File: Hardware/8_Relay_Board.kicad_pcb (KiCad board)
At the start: 4 copper layers, 74.9 x 81.3 mm, 73 parts, among them J1 Conn_01x09, J10 Screw_Terminal_3.5mm_2, J2 Conn_01x09, J3 Screw_Terminal_3.5mm_4, J4 Screw_Terminal_3.5mm_4, J5 Screw_Terminal_3.5mm_4, J6 Screw_Terminal_3.5mm_4, J7 Screw_Terminal_3.5mm_4, J8 Screw_Terminal_3.5mm_4, J9 Barrel_Jack, U1 TLP627-4, U2 TLP627-4

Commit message: Close to finishing layout
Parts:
- removed J9: Barrel_Jack, SparkFun-Connector:POWER_JACK_PTH
- added J11: USB_C_Receptacle, SparkFun-Connector:USB-C-16P, F.Cu at (168.9, 144.8)
- added R18: 5.1k, SparkFun-Resistor:R_0603_1608Metric, F.Cu at (170.2, 141.0)
- added R19: 5.1k, SparkFun-Resistor:R_0603_1608Metric, F.Cu at (167.6, 141.0)
- added U3: TLP627, SparkFun-Semiconductor-Standard:DIP4, F.Cu at (110.5, 137.2)
- added U4: TLP627, SparkFun-Semiconductor-Standard:DIP4, F.Cu at (129.5, 137.2)
- added U5: TLP627, SparkFun-Semiconductor-Standard:DIP4, F.Cu at (135.9, 137.2)
- added U6: TLP627, SparkFun-Semiconductor-Standard:DIP4, F.Cu at (142.2, 137.2)
- added U8: TLP627, SparkFun-Semiconductor-Standard:DIP4, F.Cu at (148.6, 137.2)
- added U9: TLP627, SparkFun-Semiconductor-Standard:DIP4, F.Cu at (154.9, 137.2)
- added kibuzzard-6524CD2A: G***, kibuzzard-6524CD2A, F.Cu at (101.5, 91.2)
- added kibuzzard-6524CD2A: G***, kibuzzard-6524CD2A, F.Cu at (101.5, 80.6)
- added kibuzzard-6524CD2A: G***, kibuzzard-6524CD2A, F.Cu at (183.0, 98.2)
- added kibuzzard-6524CD2A: G***, kibuzzard-6524CD2A, F.Cu at (183.0, 119.1)
- added kibuzzard-6524CD2A: G***, kibuzzard-6524CD2A, F.Cu at (183.0, 87.6)
- added kibuzzard-6524CD2A: G***, kibuzzard-6524CD2A, F.Cu at (101.5, 101.7)
- added kibuzzard-6524CD2A: G***, kibuzzard-6524CD2A, F.Cu at (183.0, 108.6)
- added kibuzzard-6524CD2A: G***, kibuzzard-6524CD2A, F.Cu at (101.5, 112.1)
- added kibuzzard-6524CD3E: G***, kibuzzard-6524CD3E, F.Cu at (101.5, 84.1)
- added kibuzzard-6524CD3E: G***, kibuzzard-6524CD3E, F.Cu at (101.5, 115.6)
- added kibuzzard-6524CD3E: G***, kibuzzard-6524CD3E, F.Cu at (101.5, 94.6)
- added kibuzzard-6524CD3E: G***, kibuzzard-6524CD3E, F.Cu at (183.0, 105.0)
- added kibuzzard-6524CD3E: G***, kibuzzard-6524CD3E, F.Cu at (101.5, 105.2)
- added kibuzzard-6524CD3E: G***, kibuzzard-6524CD3E, F.Cu at (183.0, 94.6)
- added kibuzzard-6524CD3E: G***, kibuzzard-6524CD3E, F.Cu at (183.0, 115.6)
- added kibuzzard-6524CD3E: G***, kibuzzard-6524CD3E, F.Cu at (183.0, 84.1)
- added kibuzzard-6524CD4E: G***, kibuzzard-6524CD4E, F.Cu at (183.0, 91.2)
- added kibuzzard-6524CD4E: G***, kibuzzard-6524CD4E, F.Cu at (183.0, 112.1)
- added kibuzzard-6524CD4E: G***, kibuzzard-6524CD4E, F.Cu at (101.5, 119.1)
- added kibuzzard-6524CD4E: G***, kibuzzard-6524CD4E, F.Cu at (101.5, 87.6)
- added kibuzzard-6524CD4E: G***, kibuzzard-6524CD4E, F.Cu at (101.5, 98.2)
- added kibuzzard-6524CD4E: G***, kibuzzard-6524CD4E, F.Cu at (183.0, 101.6)
- added kibuzzard-6524CD4E: G***, kibuzzard-6524CD4E, F.Cu at (101.5, 108.7)
- added kibuzzard-6524CD4E: G***, kibuzzard-6524CD4E, F.Cu at (183.0, 80.6)
- JP9: moved to B.Cu
- U1, U2: value TLP627-4 -> TLP627; footprint SparkFun-Semiconductor-Standard:PDIP16 -> SparkFun-Semiconductor-Standard:DIP4
- U7: footprint SparkFun-Aesthetic:Ordering_Instructions -> SparkFun-Aesthetic:ORDERING_INSTRUCTIONS
- moved U1 29.6 mm to (116.8, 137.2), turned to 90 degrees
- moved ST1 9.52 mm to (183.5, 73.7)
- moved ST2 9.52 mm to (183.5, 149.9)
- moved FID1 8.89 mm to (179.1, 151.1)
- moved FID4 8.89 mm to (179.1, 151.1)
- moved U2 8.13 mm to (123.2, 137.2), turned to 90 degrees
- moved R12 6.48 mm to (132.1, 141.0)
- moved J1 6.35 mm to (138.4, 151.1)
- moved J2 6.35 mm to (138.4, 148.6)
- moved JP5 5.39 mm to (148.6, 116.8)
- moved JP6 5.39 mm to (148.6, 104.1)
- moved JP7 5.39 mm to (148.6, 91.4)
- moved JP8 5.39 mm to (148.6, 78.7)
- moved R11 5.24 mm to (125.7, 141.0)
- moved J10 5.08 mm to (152.7, 148.6)
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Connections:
- J3 pad 1: NO1 -> COM1
- J3 pad 2: COM1 -> NC1
- J3 pad 3: NC1 -> NO1
- J3 pad 4: NO2 -> COM2
- J4 pad 1: COM2 -> NC2
- J4 pad 2: NC2 -> NO2
- J4 pad 3: NO3 -> COM3
- J4 pad 4: COM3 -> NC3
- J5 pad 1: NC3 -> NO3
- J5 pad 2: NO4 -> COM4
- J5 pad 3: COM4 -> NC4
- J5 pad 4: NC4 -> NO4
- J6 pad 1: NO5 -> COM5
- J6 pad 2: COM5 -> NC5
- J6 pad 3: NC5 -> NO5
- J6 pad 4: NO6 -> COM6
- J7 pad 1: COM6 -> NC6
- J7 pad 2: NC6 -> NO6
- J7 pad 3: NO7 -> COM7
- J7 pad 4: COM7 -> NC7
- J8 pad 1: NC7 -> NO7
- J8 pad 2: NO8 -> COM8
- J8 pad 3: COM8 -> NC8
- J8 pad 4: NC8 -> NO8
- U1 pad 1: IN5 -> IN2
- U1 pad 2: Net-(R13-Pad2) -> Net-(R10-Pad2)
- U1 pad 3: IN6 -> GND
- U1 pad 4: Net-(R14-Pad2) -> RELAY3
- U2 pad 1: IN1 -> IN3
- U2 pad 2: Net-(R9-Pad2) -> Net-(R11-Pad2)
- U2 pad 3: IN2 -> GND
- U2 pad 4: Net-(R10-Pad2) -> RELAY2
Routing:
- net +5V: track 20.8 -> 282.8 mm, vias 0 -> 10
- net RELAY1: track 0.00 -> 82.7 mm
- net RELAY2: track 0.00 -> 67.0 mm, vias 0 -> 1
- net RELAY8: track 0.00 -> 65.2 mm
- net RELAY3: track 0.00 -> 58.3 mm, vias 0 -> 1
- net RELAY4: track 0.00 -> 48.8 mm, vias 0 -> 1
- net RELAY7: track 0.00 -> 48.8 mm
- net RELAY6: track 0.00 -> 35.7 mm
- net NC1: track 0.00 -> 17.8 mm
- net NC8: track 0.00 -> 16.8 mm
- net NC2: track 0.00 -> 16.1 mm
- net NC7: track 0.00 -> 15.9 mm
- net RELAY5: track 0.00 -> 15.8 mm
- net NC4: track 0.00 -> 15.3 mm
- net NC3: track 0.00 -> 15.2 mm
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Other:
- board size 74.9 x 81.3 mm -> 87.6 x 81.3 mm
- board text added: "Layers: 2"
- board text removed: "Controlled Impedance: JLC7628"
- board text removed: "Finish: ENIG"
- board text removed: "Layers: 4"
- board text removed: "Material: TG155"
- board text removed: "No Clean Process"

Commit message: Ready for final review
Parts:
- removed kibuzzard-6524CD2A (x8): G***, kibuzzard-6524CD2A
- removed kibuzzard-6524CD3E (x8): G***, kibuzzard-6524CD3E
- removed kibuzzard-6524CD4E (x8): G***, kibuzzard-6524CD4E
- added G***: LOGO, SparkFun-Aesthetic:SparkX_Logo_8mm, F.Cu at (175.3, 134.4)
- added G***: LOGO, SparkFun-Aesthetic:SparkX_Logo_8mm, B.Cu at (142.2, 130.0)
- added kibuzzard-65297156: G***, kibuzzard-65297156, F.Cu at (140.7, 121.9)
- added kibuzzard-65297156: G***, kibuzzard-65297156, B.Cu at (126.2, 116.3)
- added kibuzzard-65297163: G***, kibuzzard-65297163, F.Cu at (140.2, 107.7)
- added kibuzzard-65297163: G***, kibuzzard-65297163, B.Cu at (126.0, 103.9)
- added kibuzzard-6529717D: G***, kibuzzard-6529717D, F.Cu at (140.2, 95.0)
- added kibuzzard-6529717D: G***, kibuzzard-6529717D, B.Cu at (126.0, 91.4)
- added kibuzzard-65297189: G***, kibuzzard-65297189, F.Cu at (140.2, 82.3)
- added kibuzzard-65297189: G***, kibuzzard-65297189, B.Cu at (126.0, 79.0)
- added kibuzzard-65297199: G***, kibuzzard-65297199, F.Cu at (144.8, 74.2)
- added kibuzzard-65297199: G***, kibuzzard-65297199, B.Cu at (158.8, 78.7)
- added kibuzzard-652971A7: G***, kibuzzard-652971A7, F.Cu at (144.3, 87.9)
- added kibuzzard-652971A7: G***, kibuzzard-652971A7, B.Cu at (158.8, 91.4)
- added kibuzzard-652971AD: G***, kibuzzard-652971AD, F.Cu at (144.8, 100.6)
- added kibuzzard-652971AD: G***, kibuzzard-652971AD, B.Cu at (158.8, 104.4)
- added kibuzzard-652971B3: G***, kibuzzard-652971B3, F.Cu at (144.3, 113.3)
- added kibuzzard-652971B3: G***, kibuzzard-652971B3, B.Cu at (158.8, 116.6)
- added kibuzzard-65297316: G***, kibuzzard-65297316, F.Cu at (118.1, 146.1)
- added kibuzzard-65297316: G***, kibuzzard-65297316, B.Cu at (118.1, 146.1)
- added kibuzzard-65297321: G***, kibuzzard-65297321, F.Cu at (120.7, 146.1)
- added kibuzzard-65297321: G***, kibuzzard-65297321, B.Cu at (120.7, 146.1)
- added kibuzzard-65297327: G***, kibuzzard-65297327, F.Cu at (123.2, 146.1)
- added kibuzzard-65297327: G***, kibuzzard-65297327, B.Cu at (123.2, 146.1)
- added kibuzzard-6529732E: G***, kibuzzard-6529732E, F.Cu at (125.7, 146.1)
- added kibuzzard-6529732E: G***, kibuzzard-6529732E, B.Cu at (125.7, 146.1)
- added kibuzzard-65297338: G***, kibuzzard-65297338, F.Cu at (128.3, 146.1)
- added kibuzzard-65297338: G***, kibuzzard-65297338, B.Cu at (128.3, 146.1)
- added kibuzzard-6529733E: G***, kibuzzard-6529733E, F.Cu at (130.8, 146.1)
- added kibuzzard-6529733E: G***, kibuzzard-6529733E, B.Cu at (130.8, 146.1)
- added kibuzzard-65297343: G***, kibuzzard-65297343, F.Cu at (133.3, 146.1)
- added kibuzzard-65297343: G***, kibuzzard-65297343, B.Cu at (133.3, 146.1)
- added kibuzzard-6529734A: G***, kibuzzard-6529734A, F.Cu at (135.9, 146.1)
- added kibuzzard-6529734A: G***, kibuzzard-6529734A, B.Cu at (135.9, 146.1)
- added kibuzzard-65297353: G***, kibuzzard-65297353, F.Cu at (138.4, 146.7)
- added kibuzzard-65297353: G***, kibuzzard-65297353, B.Cu at (138.4, 146.7)
- added kibuzzard-652973B2: G***, kibuzzard-652973B2, F.Cu at (130.2, 151.1)
- added kibuzzard-652973E9: G***, kibuzzard-652973E9, F.Cu at (168.9, 130.2)
- added kibuzzard-65297443: G***, kibuzzard-65297443, F.Cu at (152.7, 143.5)
- added kibuzzard-65297443: G***, kibuzzard-65297443, B.Cu at (152.7, 143.5)
- added kibuzzard-65297450: G***, kibuzzard-65297450, F.Cu at (156.2, 143.5)
- added kibuzzard-65297450: G***, kibuzzard-65297450, B.Cu at (156.2, 143.5)
- added kibuzzard-65298D3A: G***, kibuzzard-65298D3A, F.Cu at (161.3, 148.8)
- added kibuzzard-65298D3A: G***, kibuzzard-65298D3A, B.Cu at (161.0, 148.8)
- added kibuzzard-652991A0: G***, kibuzzard-652991A0, B.Cu at (130.3, 151.1)
- added kibuzzard-652997F8: G***, kibuzzard-652997F8, F.Cu at (179.3, 134.6)
- added kibuzzard-65299803: G***, kibuzzard-65299803, F.Cu at (182.4, 134.6)
- added kibuzzard-6529980A: G***, kibuzzard-6529980A, B.Cu at (142.0, 134.1)
- added kibuzzard-65299816: G***, kibuzzard-65299816, B.Cu at (142.0, 137.2)
- U1, U2, U3, U4, U5, U6, U8, U9: footprint SparkFun-Semiconductor-Standard:DIP4 -> SparkFun-Semiconductor-Standard:SMDIP4
- moved U3 4.02 mm to (111.8, 133.3)
- moved U4 4.02 mm to (130.8, 133.3)
- moved U5 4.02 mm to (137.2, 133.3)
- moved U8 4.02 mm to (149.9, 133.3)
- moved U9 4.02 mm to (156.2, 133.3)
- moved U1 4.02 mm to (118.1, 133.3)
- moved U2 4.02 mm to (124.5, 133.3)
- moved U6 4.02 mm to (143.5, 133.3)
- moved J1 2.54 mm to (138.4, 148.6)
- moved J2 2.54 mm to (138.4, 151.1)
- moved J11 1.21 mm to (168.9, 146.0)
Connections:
- J3 pad 1: COM1 -> NC1
- J3 pad 2: NC1 -> COM1
- J3 pad 4: COM2 -> NC2
- J4 pad 1: NC2 -> COM2
- J4 pad 3: COM3 -> NC3
- J4 pad 4: NC3 -> COM3
- J5 pad 2: COM4 -> NC4
- J5 pad 3: NC4 -> COM4
- J6 pad 1: COM5 -> NC5
- J6 pad 2: NC5 -> COM5
- J6 pad 4: COM6 -> NC6
- J7 pad 1: NC6 -> COM6
- J7 pad 3: COM7 -> NC7
- J7 pad 4: NC7 -> COM7
- J8 pad 2: COM8 -> NC8
- J8 pad 3: NC8 -> COM8
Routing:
- net +5V: track 282.8 -> 287.8 mm
- net COM1: track 12.3 -> 15.9 mm
- net IN3: track 14.9 -> 11.4 mm
- net GND: track 1.85 -> 4.94 mm
- net COM8: track 13.3 -> 10.3 mm
- net IN2: track 15.5 -> 13.0 mm
- net IN7: track 25.5 -> 23.0 mm
- net IN4: track 15.5 -> 13.0 mm
- net NC1: track 17.8 -> 15.9 mm
- net IN6: track 20.9 -> 19.1 mm
- net NC4: track 15.3 -> 16.7 mm
- net NC8: track 16.8 -> 18.2 mm
- net COM3: track 10.4 -> 11.9 mm
- net COM2: track 11.3 -> 12.8 mm
- net COM5: track 10.3 -> 11.7 mm
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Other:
- board text added: "x01"

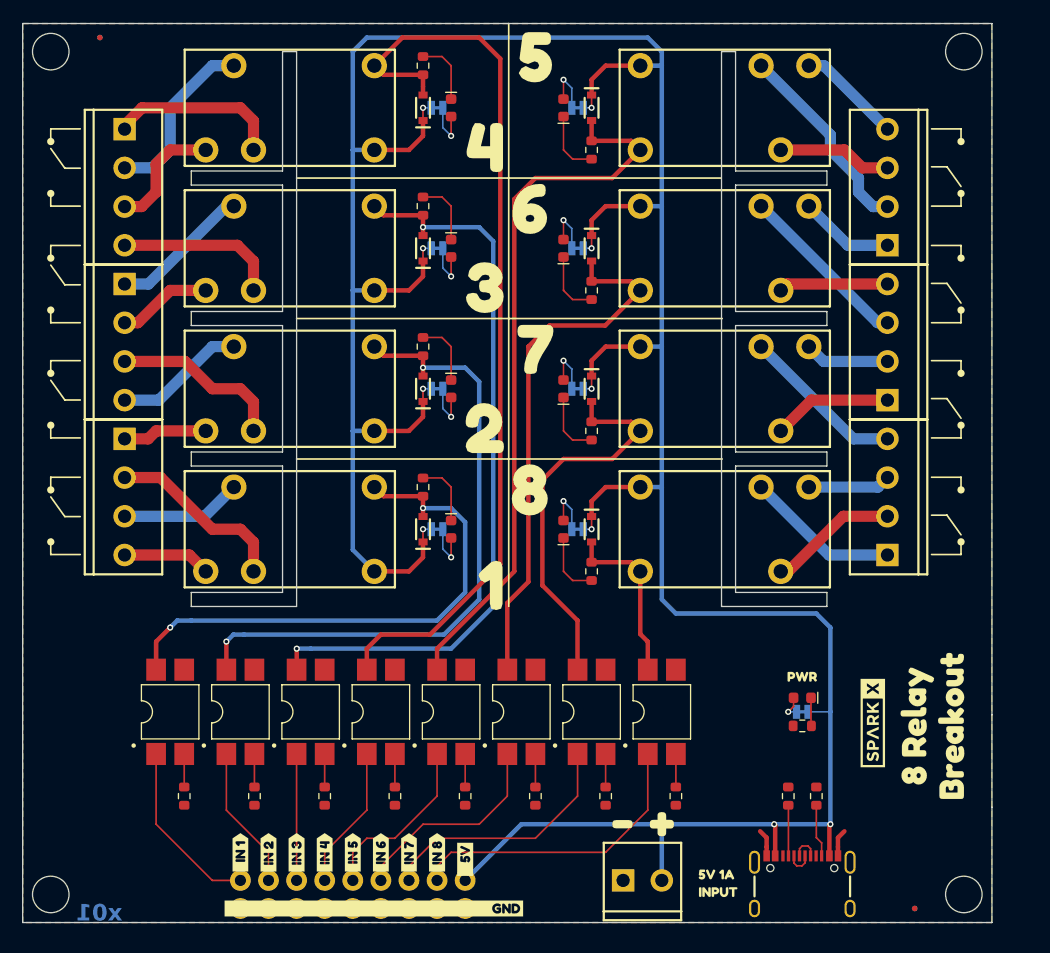
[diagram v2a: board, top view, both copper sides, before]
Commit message: Second pre-release revision
- Add isolation under relays
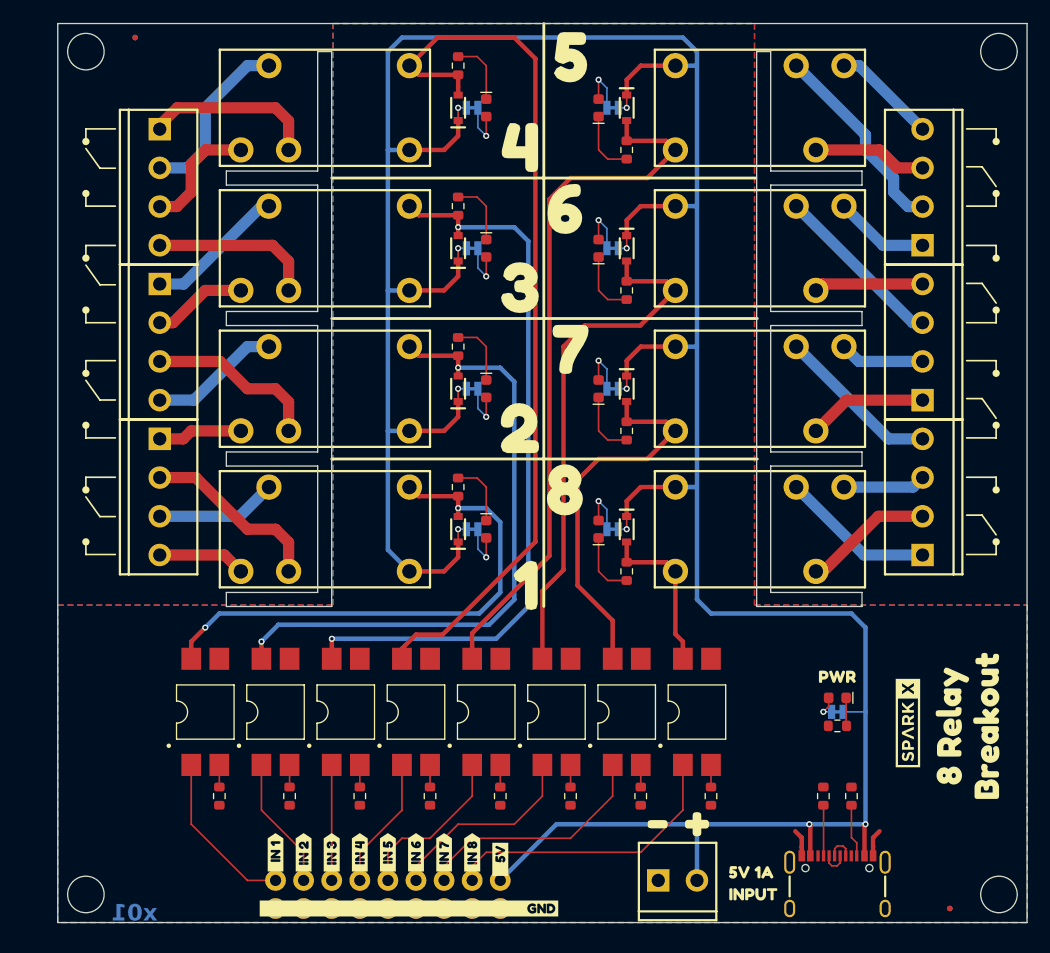
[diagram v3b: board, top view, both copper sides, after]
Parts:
- removed the kibuzzard-6529734A at (135.9, 146.1)
- removed kibuzzard-652973E9: G***, kibuzzard-652973E9
- removed kibuzzard-65298D3A (x2): G***, kibuzzard-65298D3A
- added kibuzzard-652EF841: G***, kibuzzard-652EF841, F.Cu at (139.1, 146.1)
- added kibuzzard-652EF889: G***, kibuzzard-652EF889, F.Cu at (164.5, 148.8)
- added kibuzzard-652EF88E: G***, kibuzzard-652EF88E, B.Cu at (164.2, 148.8)
- added kibuzzard-65656C10: G***, kibuzzard-65656C10, F.Cu at (172.1, 130.2)
- added kibuzzard-65656C50: G***, kibuzzard-65656C50, B.Cu at (172.1, 130.0)
- added kibuzzard-65656C62: G***, kibuzzard-65656C62, B.Cu at (151.6, 89.4)
- added kibuzzard-65656C62: G***, kibuzzard-65656C62, B.Cu at (138.9, 76.7)
- added kibuzzard-65656C62: G***, kibuzzard-65656C62, B.Cu at (151.8, 76.7)
- added kibuzzard-65656C62: G***, kibuzzard-65656C62, B.Cu at (138.9, 114.8)
- added kibuzzard-65656C62: G***, kibuzzard-65656C62, B.Cu at (151.6, 102.1)
- added kibuzzard-65656C62: G***, kibuzzard-65656C62, B.Cu at (138.9, 89.4)
- added kibuzzard-65656C62: G***, kibuzzard-65656C62, B.Cu at (138.9, 102.1)
- added kibuzzard-65656C62: G***, kibuzzard-65656C62, B.Cu at (151.6, 114.8)
- JP1, JP2, JP3, JP4, JP5, JP6, JP7, JP8, JP9: footprint SparkFun-Jumper:SMT-JUMPER_2_NC_TRACE_NO-SILK -> SparkFun-Jumper:SMT-JUMPER_2_NC_TRACE_SILK
- U1: renamed from U3; value TLP627 -> SFH619A-SMT; footprint SparkFun-Semiconductor-Standard:SMDIP4 -> SparkFun-Semiconductor-Standard:SMDIP4-WIDE
- U2: renamed from U1; value TLP627 -> SFH619A-SMT; footprint SparkFun-Semiconductor-Standard:SMDIP4 -> SparkFun-Semiconductor-Standard:SMDIP4-WIDE
- U3: renamed from U2; value TLP627 -> SFH619A-SMT; footprint SparkFun-Semiconductor-Standard:SMDIP4 -> SparkFun-Semiconductor-Standard:SMDIP4-WIDE
- U4, U5, U6: value TLP627 -> SFH619A-SMT; footprint SparkFun-Semiconductor-Standard:SMDIP4 -> SparkFun-Semiconductor-Standard:SMDIP4-WIDE
- U7: renamed from U8; value TLP627 -> SFH619A-SMT; footprint SparkFun-Semiconductor-Standard:SMDIP4 -> SparkFun-Semiconductor-Standard:SMDIP4-WIDE
- U8: renamed from U9; value TLP627 -> SFH619A-SMT; footprint SparkFun-Semiconductor-Standard:SMDIP4 -> SparkFun-Semiconductor-Standard:SMDIP4-WIDE
- moved D11 3.18 mm to (150.5, 104.1)
- moved D13 3.18 mm to (150.5, 91.4)
- moved D15 3.18 mm to (150.5, 78.7)
- moved D17 3.18 mm to (172.1, 132.1)
- moved D2 3.18 mm to (140.3, 91.4)
- moved D4 3.18 mm to (140.3, 104.1)
- moved D6 3.18 mm to (140.3, 116.8)
- moved D8 3.18 mm to (150.5, 116.8)
- moved D9 3.18 mm to (140.3, 78.7)
- moved FID1 3.18 mm to (182.2, 151.1)
- moved FID4 3.18 mm to (182.2, 151.1)
- moved G*** 3.18 mm to (178.4, 134.4)
- moved G1 3.18 mm to (235.6, 174.0)
- moved J11 3.18 mm to (172.1, 146.0)
- moved JP1 3.18 mm to (139.1, 78.7)
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- renumbered K4 to K1, K3 to K2, K2 to K3, K1 to K4, K8 to K5, K7 to K6, K6 to K7, K5 to K8, U7 to U9
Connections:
- D1 pad A: RELAY1 -> RELAY4
- D10 pad A: RELAY5 -> RELAY8
- D12 pad A: RELAY6 -> RELAY7
- D14 pad A: RELAY7 -> RELAY6
- D16 pad A: RELAY8 -> RELAY5
- D3 pad A: RELAY2 -> RELAY3
- D5 pad A: RELAY3 -> RELAY2
- D7 pad A: RELAY4 -> RELAY1
- K1 pad 2: RELAY4 -> RELAY1
- K2 pad 2: RELAY3 -> RELAY2
- K3 pad 2: RELAY2 -> RELAY3
- K4 pad 2: RELAY1 -> RELAY4
- K5 pad 2: RELAY8 -> RELAY5
- K6 pad 2: RELAY7 -> RELAY6
- K7 pad 2: RELAY6 -> RELAY7
- K8 pad 2: RELAY5 -> RELAY8
- R1 pad 2: RELAY1 -> RELAY4
- R2 pad 2: RELAY2 -> RELAY3
- R3 pad 2: RELAY3 -> RELAY2
- R4 pad 2: RELAY4 -> RELAY1
- R5 pad 2: RELAY5 -> RELAY8
- R6 pad 2: RELAY6 -> RELAY7
- R7 pad 2: RELAY7 -> RELAY6
- R8 pad 2: RELAY8 -> RELAY5
- U1 pad 4: RELAY4 -> RELAY1
- U2 pad 4: RELAY3 -> RELAY2
- U3 pad 4: RELAY2 -> RELAY3
- U4 pad 4: RELAY1 -> RELAY4
- U5 pad 4: RELAY8 -> RELAY5
- U6 pad 4: RELAY7 -> RELAY6
- U7 pad 4: RELAY6 -> RELAY7
- U8 pad 4: RELAY5 -> RELAY8
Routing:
- net RELAY8: track 65.2 -> 14.8 mm
- net RELAY5: track 15.8 -> 64.3 mm
- net RELAY1: track 82.7 -> 48.6 mm, vias 0 -> 2
- net RELAY4: track 49.6 -> 80.5 mm, vias 2 -> 0
- net RELAY7: track 48.8 -> 34.7 mm
- net RELAY6: track 35.7 -> 47.8 mm
- net RELAY2: track 67.7 -> 57.9 mm
- net RELAY3: track 58.8 -> 67.3 mm
- net IN7: track 23.0 -> 22.0 mm
- net IN6: track 19.1 -> 18.2 mm
- net IN1: track 16.1 -> 15.1 mm
- net Net-(R9-Pad2): track 2.99 -> 2.00 mm
- net Net-(R16-Pad2): track 2.99 -> 2.00 mm
- net Net-(R15-Pad2): track 2.99 -> 2.00 mm
- net Net-(R14-Pad2): track 2.99 -> 2.00 mm
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
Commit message: Add docs zip and schematic pdf
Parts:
- moved U9 4.22 mm to (221.2, 114.8)
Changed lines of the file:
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@@
   )
   (footprint "SparkFun-Aesthetic:ORDERING_INSTRUCTIONS" (layer "F.Cu")
-    (at 224.2292 111.835)
+    (at 221.234 114.808)
     (property "Sheetfile" "8_Relay_Board.kicad_sch")
     (property "Sheetname" "")
@@
     (effects (font (size 1.5 1.5) (thickness 0.3) bold) (justify bottom))
   )
-  (gr_text "Layers: 2\n" (at 225.450092 123.20559) (layer "F.Fab")
+  (gr_text "Layers: 2\n" (at 222.454892 126.17859) (layer "F.Fab")
     (effects (font (size 2 2) (thickness 0.15)) (justify left bottom))
   )
-  (gr_text "Solder Mask: Red" (at 225.450092 120.66559) (layer "F.Fab")
+  (gr_text "Solder Mask: Red" (at 222.454892 123.63859) (layer "F.Fab")
     (effects (font (size 2 2) (thickness 0.15)) (justify left bottom))
   )
-  (gr_text "Thickness: 1.6mm" (at 225.806 126.111) (layer "F.Fab")
+  (gr_text "Thickness: 1.6mm" (at 222.8108 129.084) (layer "F.Fab")
     (effects (font (size 2 2) (thickness 0.15)) (justify left bottom))
   )
